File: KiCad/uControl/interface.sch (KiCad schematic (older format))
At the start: 41 parts, among them P10 C3SB, P11 VSel_Vlv, P12 Valve_Conn, P13 Valve_Conn_BO, P14 Valve, P15 Flow_Conn, P16 FlowMeter, P17 Pump_Conn, P18 Pump_Conn_BO, P19 Pump_Conn_Flex, P20 Temp_Conn, P21 Temp_Conn_BO, P22 Temp, P23 Pump, P6 Pulse, P7 Gage_Pr, P8 Abso_Pr, P9 C3SB, Q1 2SD1834T100, U1 TXB0104D, U2 TXS0102DCT

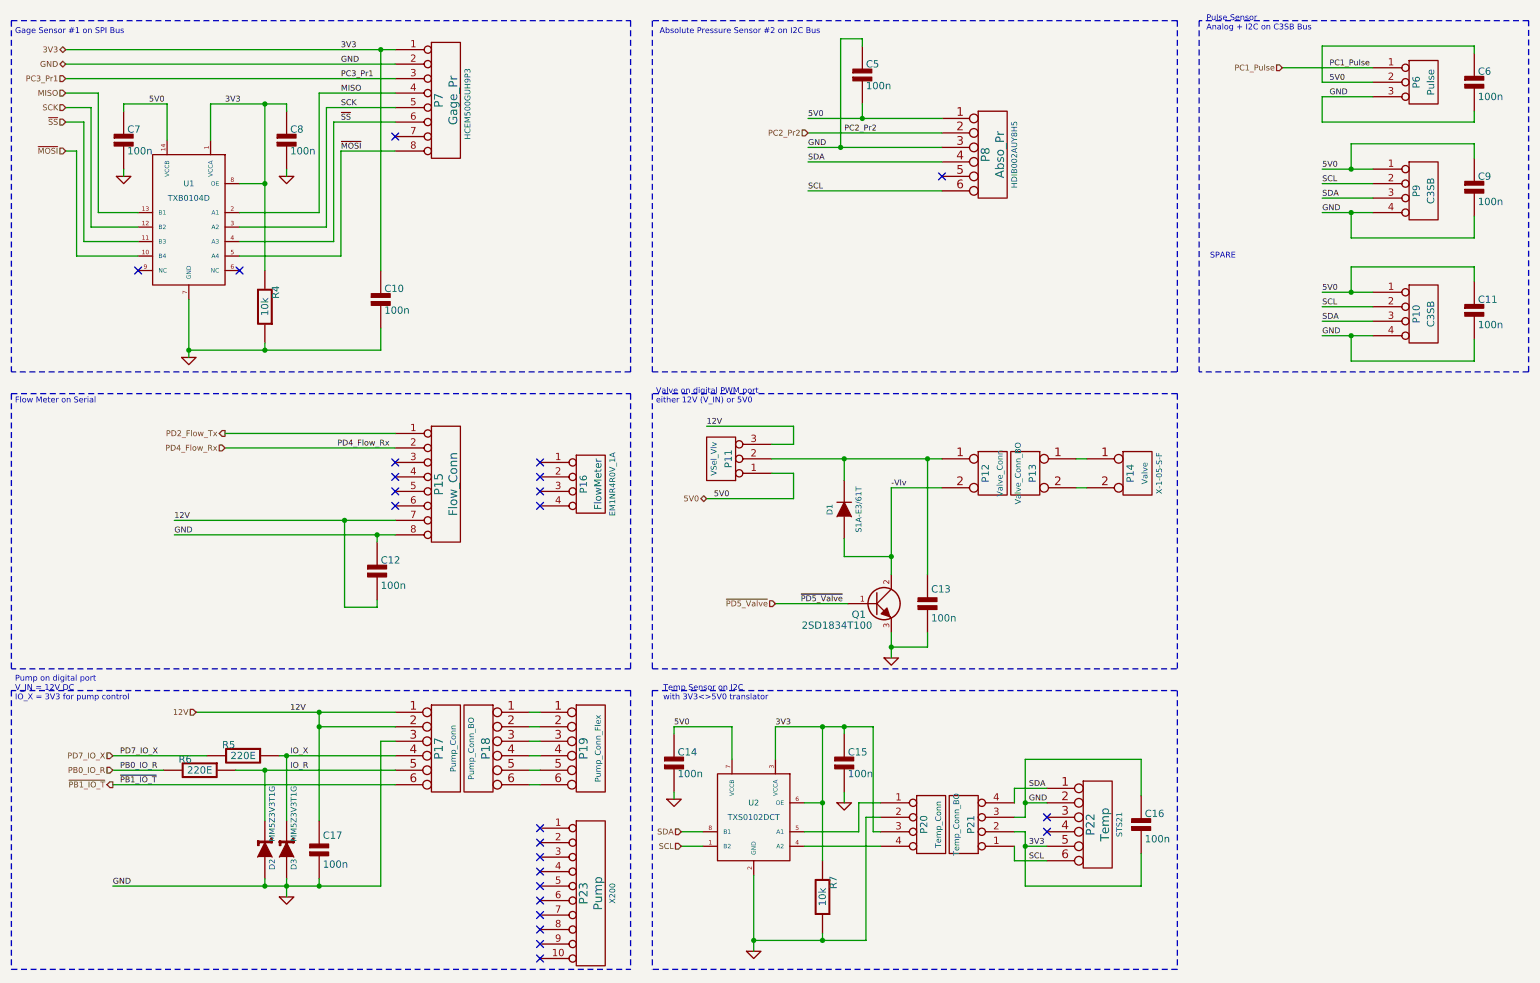
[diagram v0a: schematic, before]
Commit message: uControl footprints done. working on initial board layout
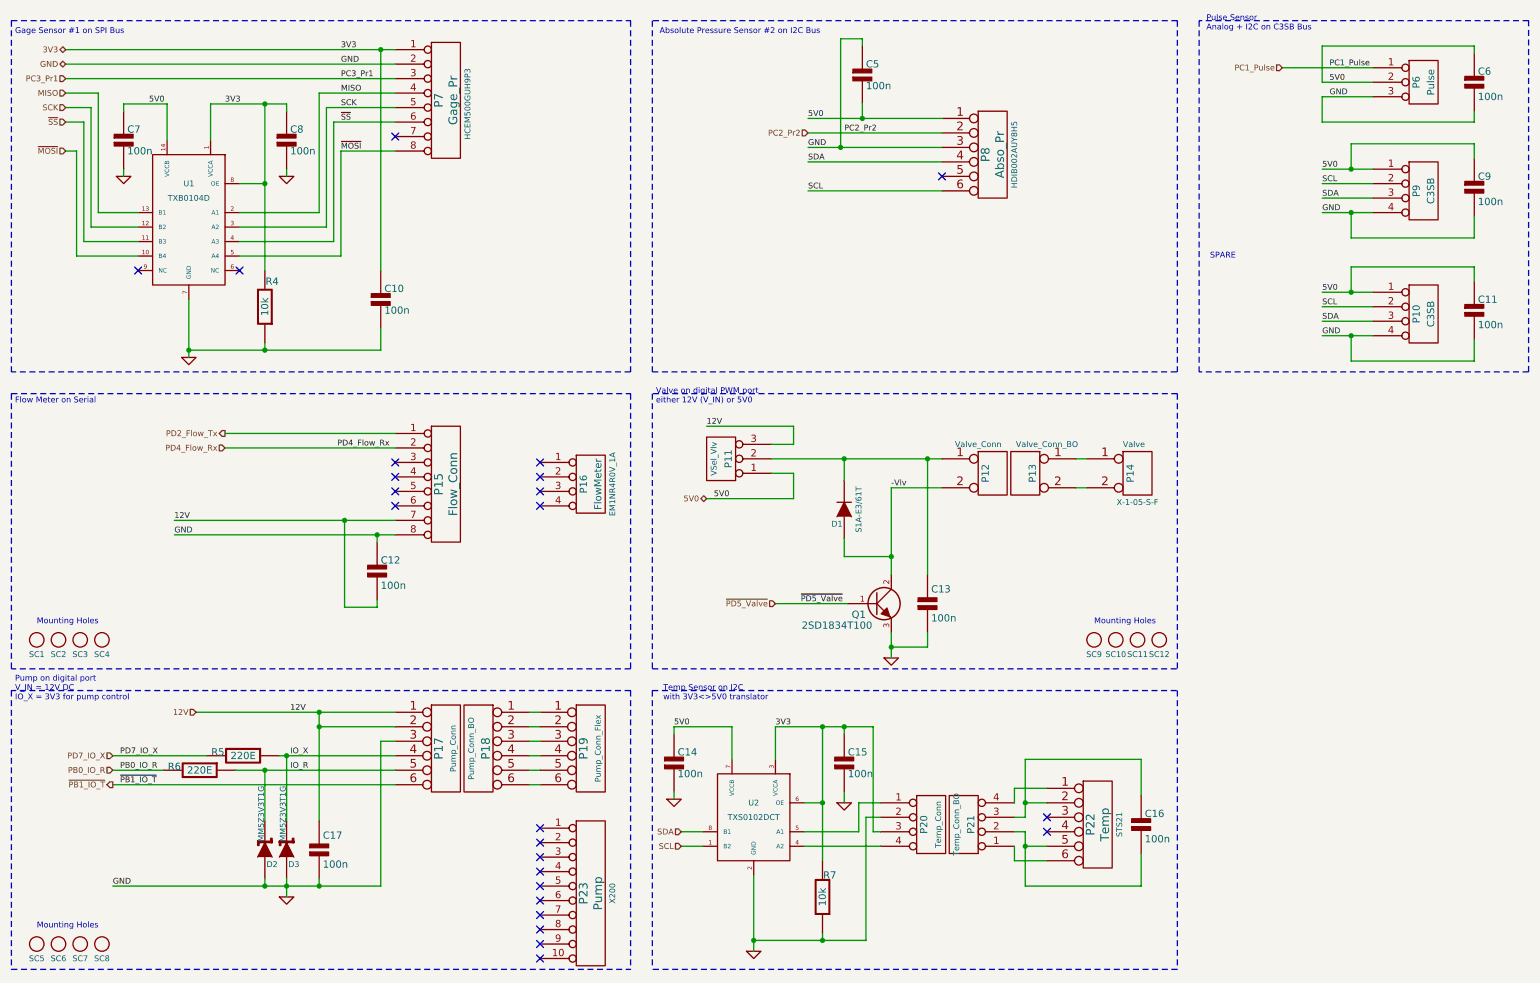
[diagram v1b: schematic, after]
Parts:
- added SC1, SC10, SC11, SC12, SC2, SC3, SC4, SC5, SC6, SC7, SC8, SC9: SCREW, vite_3mm, symbol SCREW
- D1: footprint diode-DO214AA -> S1A-E3
- D2, D3: footprint diode-DO214AA -> MM5Z3V3T1G
- P20, P21: footprint SIL-4 -> Header_2x2
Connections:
- net 3V3: no longer C16.2, P21.2 (P2), P22.5
- net GND: no longer C16.1, P21.3 (P3), P22.2
- net SCL: no longer P21.1 (P1), P22.6
- net SDA: no longer P21.4 (P4), P22.1
- new net: P21.4 (P4), P22.1
- new net: C16.1, P21.3 (P3), P22.2
- new net: C16.2, P21.2 (P2), P22.5
- new net: P21.1 (P1), P22.6
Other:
- note added: "Mounting Holes"
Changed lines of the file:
@@
-EESchema Schematic File Version 2  date Monday 24 December 2012 10:32:09 PM IST
+EESchema Schematic File Version 2  date 12/25/2012 5:14:27 PM
 LIBS:uControl
 LIBS:Conn-raspberry
@@
 Sheet 2 5
 Title ""
-Date "24 dec 2012"
+Date "25 dec 2012"
 Rev ""
 Comp ""
@@
 Comment4 ""
 $EndDescr
+$Comp
+L SCREW SC9
+U 1 1 50D99159
+P 8150 4850
+F 0 "SC9" H 8150 4750 40  0000 C CNN
+F 1 "SCREW" H 8150 4950 40  0001 C CNN
+F 2 "vite_3mm" H 8150 5050 40  0001 C CNN
+	1    8150 4850
+	1    0    0    -1
+$EndComp
+$Comp
+L SCREW SC10
+U 1 1 50D99158
+P 8300 4850
+F 0 "SC10" H 8300 4750 40  0000 C CNN
+F 1 "SCREW" H 8300 4950 40  0001 C CNN
+F 2 "vite_3mm" H 8300 5050 40  0001 C CNN
+	1    8300 4850
+	1    0    0    -1
+$EndComp
+$Comp
+L SCREW SC11
+U 1 1 50D99157
+P 8450 4850
+F 0 "SC11" H 8450 4750 40  0000 C CNN
+F 1 "SCREW" H 8450 4950 40  0001 C CNN
+F 2 "vite_3mm" H 8450 5050 40  0001 C CNN
+	1    8450 4850
+	1    0    0    -1
+$EndComp
+$Comp
+L SCREW SC12
+U 1 1 50D99156
+P 8600 4850
+F 0 "SC12" H 8600 4750 40  0000 C CNN
+F 1 "SCREW" H 8600 4950 40  0001 C CNN
+F 2 "vite_3mm" H 8600 5050 40  0001 C CNN
+	1    8600 4850
+	1    0    0    -1
+$EndComp
+Text Notes 8150 4750 0    40   ~ 0
+Mounting Holes
+$Comp
+L SCREW SC5
+U 1 1 50D99149
+P 850 6950
+F 0 "SC5" H 850 6850 40  0000 C CNN
+F 1 "SCREW" H 850 7050 40  0001 C CNN
+F 2 "vite_3mm" H 850 7150 40  0001 C CNN
+	1    850  6950
+	1    0    0    -1
+$EndComp
+$Comp
+L SCREW SC6
+U 1 1 50D99148
+P 1000 6950
+F 0 "SC6" H 1000 6850 40  0000 C CNN
+F 1 "SCREW" H 1000 7050 40  0001 C CNN
+F 2 "vite_3mm" H 1000 7150 40  0001 C CNN
+	1    1000 6950
+	1    0    0    -1
+$EndComp
+$Comp
+L SCREW SC7
+U 1 1 50D99147
+P 1150 6950
+F 0 "SC7" H 1150 6850 40  0000 C CNN
+F 1 "SCREW" H 1150 7050 40  0001 C CNN
+F 2 "vite_3mm" H 1150 7150 40  0001 C CNN
+	1    1150 6950
+	1    0    0    -1
+$EndComp
+$Comp
+L SCREW SC8
+U 1 1 50D99146
+P 1300 6950
+F 0 "SC8" H 1300 6850 40  0000 C CNN
+F 1 "SCREW" H 1300 7050 40  0001 C CNN
+F 2 "vite_3mm" H 1300 7150 40  0001 C CNN
+	1    1300 6950
+	1    0    0    -1
+$EndComp
+Text Notes 850  6850 0    40   ~ 0
+Mounting Holes
+Text Notes 850  4750 0    40   ~ 0
+Mounting Holes
+$Comp
+L SCREW SC4
+U 1 1 50D990FE
+P 1300 4850
+F 0 "SC4" H 1300 4750 40  0000 C CNN
+F 1 "SCREW" H 1300 4950 40  0001 C CNN
+F 2 "vite_3mm" H 1300 5050 40  0001 C CNN
+	1    1300 4850
+	1    0    0    -1
+$EndComp
+$Comp
+L SCREW SC3
+U 1 1 50D990FC
+P 1150 4850
+F 0 "SC3" H 1150 4750 40  0000 C CNN
+F 1 "SCREW" H 1150 4950 40  0001 C CNN
+F 2 "vite_3mm" H 1150 5050 40  0001 C CNN
+	1    1150 4850
+	1    0    0    -1
+$EndComp
+$Comp
+L SCREW SC2
+U 1 1 50D990F9
+P 1000 4850
+F 0 "SC2" H 1000 4750 40  0000 C CNN
+F 1 "SCREW" H 1000 4950 40  0001 C CNN
+F 2 "vite_3mm" H 1000 5050 40  0001 C CNN
+	1    1000 4850
+	1    0    0    -1
+$EndComp
+$Comp
+L SCREW SC1
+U 1 1 50D990F0
+P 850 4850
+F 0 "SC1" H 850 4750 40  0000 C CNN
+F 1 "SCREW" H 850 4950 40  0001 C CNN
+F 2 "vite_3mm" H 850 5050 40  0001 C CNN
+	1    850  4850
+	1    0    0    -1
+$EndComp
 Wire Wire Line
 	8025 3800 8100 3800
@@
 P 8450 3700
 F 0 "P14" V 8400 3700 50  0000 C CNN
-F 1 "Valve" V 8500 3700 40  0000 C CNN
+F 1 "Valve" H 8425 3900 40  0000 C CNN
 F 2 "Valve" V 8600 3700 40  0001 C CNN
-F 4 "X-1-05-S-F" V 8600 3700 40  0000 C CNN "Part_No"
+F 4 "X-1-05-S-F" H 8450 3500 40  0000 C CNN "Part_No"
 	1    8450 3700
 	1    0    0    -1
@@
 P 7675 3700
 F 0 "P13" V 7625 3700 50  0000 C CNN
-F 1 "Valve_Conn_BO" V 7725 3700 40  0000 C CNN
+F 1 "Valve_Conn_BO" H 7525 3900 40  0000 C CNN
 F 2 "Header_5V_Link" V 7825 3700 40  0001 C CNN
 F 4 "X-1-05-S-F" V 7825 3700 40  0001 C CNN "Part_No"
@@
 P 7450 3700
 F 0 "P12" V 7400 3700 50  0000 C CNN
-F 1 "Valve_Conn" V 7500 3700 40  0000 C CNN
+F 1 "Valve_Conn" H 7350 3900 40  0000 C CNN
 F 2 "Header_5V_Link" V 7600 3700 40  0001 C CNN
 F 4 "X-1-05-S-F" V 7600 3700 40  0001 C CNN "Part_No"
@@
 F 0 "P21" V 7200 6125 50  0000 C CNN
 F 1 "Temp_Conn_BO" V 7300 6125 40  0000 C CNN
-F 2 "SIL-4" V 7400 6125 40  0001 C CNN
+F 2 "Header_2x2" V 7400 6125 40  0001 C CNN
 	1    7250 6125
 	-1   0    0    1
@@
 F 0 "P20" V 6975 6125 50  0000 C CNN
 F 1 "Temp_Conn" V 7075 6125 40  0000 C CNN
-F 2 "SIL-4" V 7175 6125 40  0001 C CNN
+F 2 "Header_2x2" V 7175 6125 40  0001 C CNN
 	1    7025 6125
 	1    0    0    -1
@@
 U 1 1 50CCC247
 P 6275 6625
-F 0 "R7" V 6200 6525 50  0000 C CNN
+F 0 "R7" H 6225 6475 50  0000 C CNN
 F 1 "10k" V 6275 6625 50  0000 C CNN
 F 2 "r_0805" V 6375 6625 50  0001 C CNN
@@
 U 1 1 50CCC15C
 P 2425 2550
-F 0 "R4" V 2350 2450 50  0000 C CNN
+F 0 "R4" H 2375 2375 50  0000 C CNN
 F 1 "10k" V 2425 2550 50  0000 C CNN
 F 2 "r_0805" V 2525 2550 50  0001 C CNN
@@
 Text HLabel 9450 900  0    40   Input ~ 0
 PC1_Pulse
-Text Label 7700 6375 0    40   ~ 0
-SCL
-Text Label 7700 5875 0    40   ~ 0
-SDA
 NoConn ~ 7825 6175
 NoConn ~ 7825 6075
@@
 	1    0    0    -1
 $EndComp
-Text Label 7700 5975 0    40   ~ 0
-GND
-Text Label 7700 6275 0    40   ~ 0
-3V3
 Text Label 9775 900  0    40   ~ 0
 PC1_Pulse
@@
 U 1 1 50BA3BBD
 P 2425 6300
-F 0 "D2" H 2325 6250 40  0000 C CNN
-F 1 "MM5Z3V3T1G" H 2675 6250 40  0000 C CNN
-F 2 "diode-DO214AA" H 2675 6350 40  0001 C CNN
+F 0 "D2" V 2325 6250 40  0000 C CNN
+F 1 "MM5Z3V3T1G" H 2675 6325 40  0000 C CNN
+F 2 "MM5Z3V3T1G" H 2675 6350 40  0001 C CNN
 	1    2425 6300
 	0    -1   -1   0
@@
 U 1 1 50BA3B80
 P 1975 5750
-F 0 "R6" V 1900 5650 50  0000 C CNN
+F 0 "R6" V 1950 5575 50  0000 C CNN
 F 1 "220E" V 1975 5750 50  0000 C CNN
 F 2 "r_0805" V 2075 5750 50  0001 C CNN
@@
 U 1 1 50B7155C
 P 6425 3950
-F 0 "D1" H 6425 4050 40  0000 C CNN
+F 0 "D1" V 6325 4000 40  0000 C CNN
 F 1 "S1A-E3/61T" H 6425 3850 40  0000 C CNN
-F 2 "diode-DO214AA" H 6425 3950 40  0001 C CNN
+F 2 "S1A-E3" H 6425 3950 40  0001 C CNN
 	1    6425 3950
 	0    -1   -1   0
@@
 U 1 1 50B22950
 P 2275 5650
-F 0 "R5" V 2200 5550 50  0000 C CNN
+F 0 "R5" V 2250 5475 50  0000 C CNN
 F 1 "220E" V 2275 5650 50  0000 C CNN
 F 2 "r_0805" V 2375 5650 50  0001 C CNN
@@
 U 1 1 50B22921
 P 2575 6300
-F 0 "D3" H 2475 6250 40  0000 C CNN
-F 1 "MM5Z3V3T1G" H 2825 6250 40  0000 C CNN
-F 2 "diode-DO214AA" H 2825 6350 40  0001 C CNN
+F 0 "D3" V 2475 6250 40  0000 C CNN
+F 1 "MM5Z3V3T1G" H 2825 6325 40  0000 C CNN
+F 2 "MM5Z3V3T1G" H 2825 6350 40  0001 C CNN
 	1    2575 6300
 	0    -1   -1   0

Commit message: uControl Board sizes defined. Manifold added. Can be single large board or smaller one with breakouts - both possible.
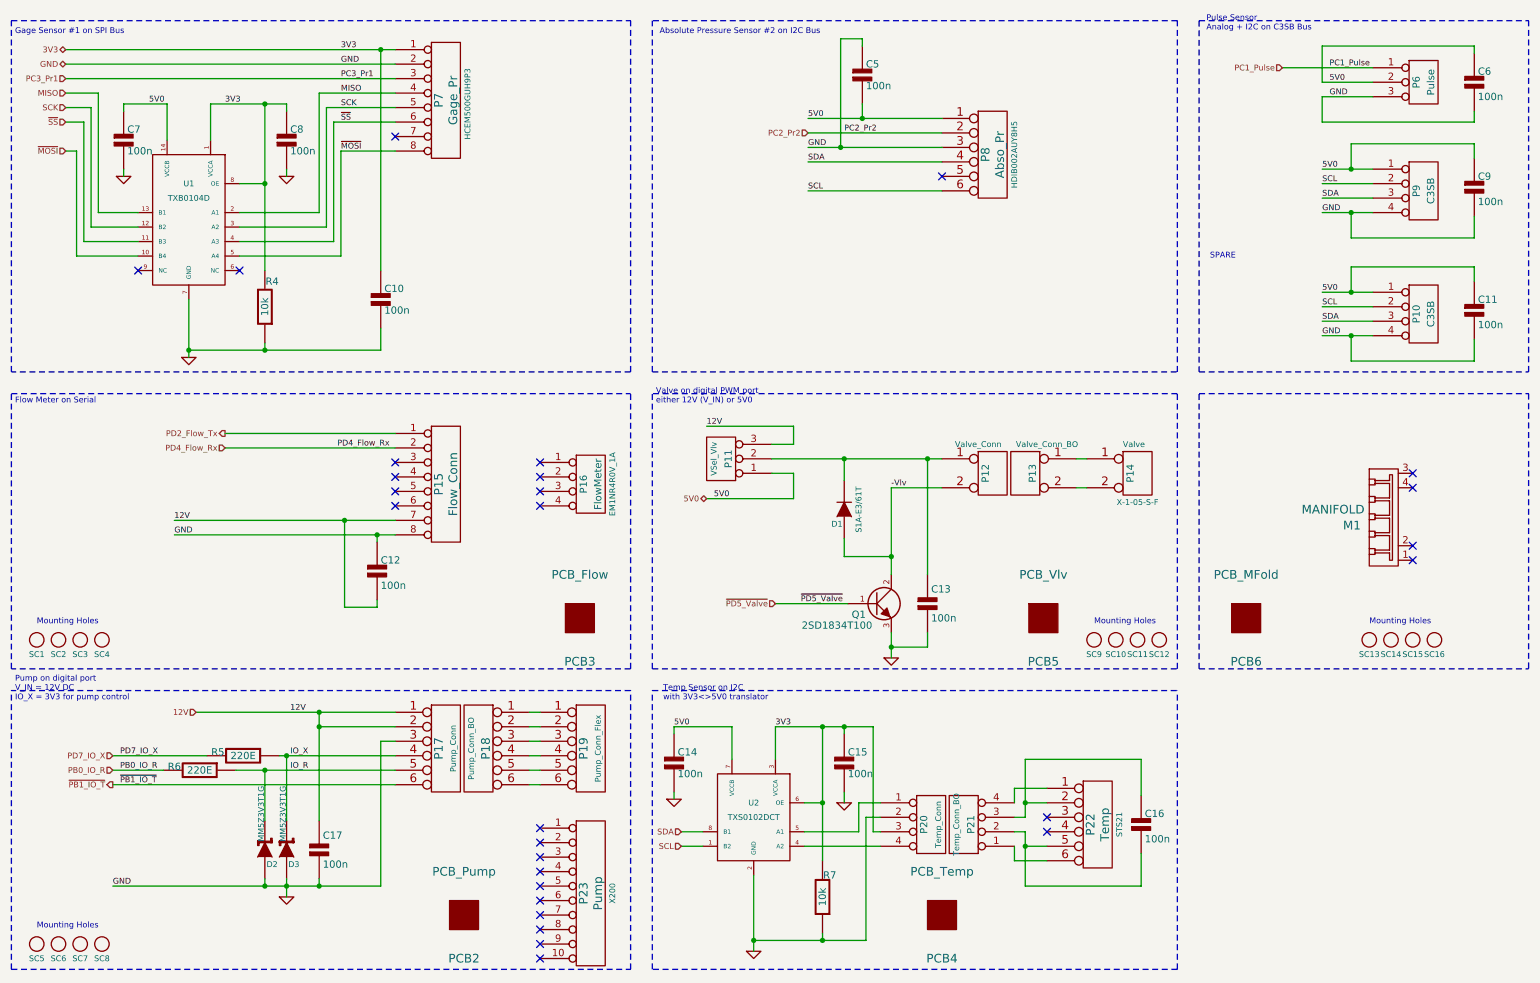
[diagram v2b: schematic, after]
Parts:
- added M1: MANIFOLD, Manifold, symbol MANIFOLD
- added PCB2: PCB_Pump, PCB_Pump, symbol PCB
- added PCB3: PCB_Flow, PCB_Flow, symbol PCB
- added PCB4: PCB_Temp, PCB_Temp, symbol PCB
- added PCB5: PCB_Vlv, PCB_Vlv, symbol PCB
- added PCB6: PCB_MFold, PCB_Mfold, symbol PCB
- added SC13, SC14, SC15, SC16: SCREW, vite_3mm, symbol SCREW
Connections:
- no-connect marks 24 -> 28

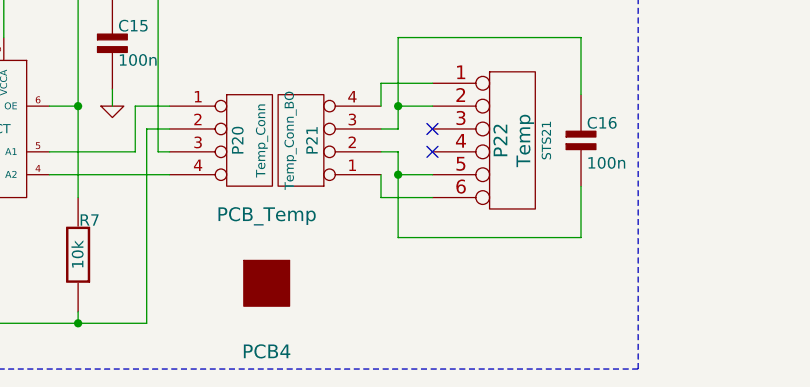
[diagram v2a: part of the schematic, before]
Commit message: uControl footprint layout almost done.
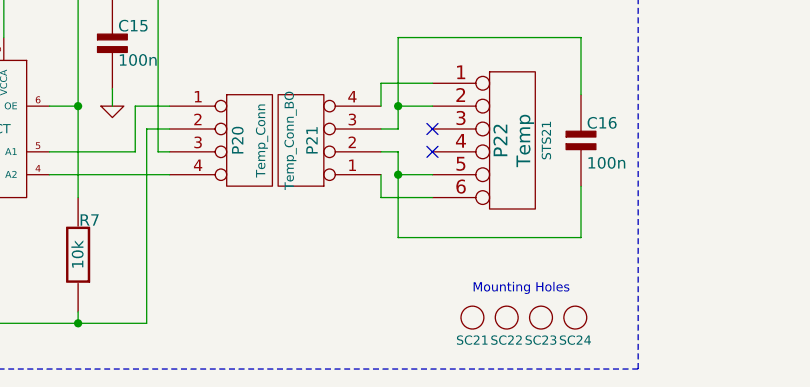
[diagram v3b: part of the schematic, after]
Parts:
- removed PCB4: PCB_Temp, PCB_Temp, symbol PCB
- added SC21, SC22, SC23, SC24: SCREW, vite_3mm, symbol SCREW
- M1: footprint Manifold -> Manifold2
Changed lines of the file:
@@
-EESchema Schematic File Version 2  date 12/26/2012 6:01:00 PM
+EESchema Schematic File Version 2  date 12/27/2012 6:53:46 PM
 LIBS:uControl
 LIBS:Conn-raspberry
@@
 Sheet 2 5
 Title ""
-Date "26 dec 2012"
+Date "27 dec 2012"
 Rev ""
 Comp ""
@@
 $EndDescr
 $Comp
+L SCREW SC21
+U 1 1 50DC1602
+P 8000 6900
+F 0 "SC21" H 8000 6800 40  0000 C CNN
+F 1 "SCREW" H 8000 7000 40  0001 C CNN
+F 2 "vite_3mm" H 8000 7100 40  0001 C CNN
+	1    8000 6900
+	1    0    0    -1
+$EndComp
+$Comp
+L SCREW SC22
+U 1 1 50DC1601
+P 8150 6900
+F 0 "SC22" H 8150 6800 40  0000 C CNN
+F 1 "SCREW" H 8150 7000 40  0001 C CNN
+F 2 "vite_3mm" H 8150 7100 40  0001 C CNN
+	1    8150 6900
+	1    0    0    -1
+$EndComp
+$Comp
+L SCREW SC23
+U 1 1 50DC1600
+P 8300 6900
+F 0 "SC23" H 8300 6800 40  0000 C CNN
+F 1 "SCREW" H 8300 7000 40  0001 C CNN
+F 2 "vite_3mm" H 8300 7100 40  0001 C CNN
+	1    8300 6900
+	1    0    0    -1
+$EndComp
+$Comp
+L SCREW SC24
+U 1 1 50DC15FF
+P 8450 6900
+F 0 "SC24" H 8450 6800 40  0000 C CNN
+F 1 "SCREW" H 8450 7000 40  0001 C CNN
+F 2 "vite_3mm" H 8450 7100 40  0001 C CNN
+	1    8450 6900
+	1    0    0    -1
+$EndComp
+Text Notes 8000 6800 0    40   ~ 0
+Mounting Holes
+$Comp
 L PCB PCB6
 U 1 1 50DAE3BE
@@
 $EndComp
 $Comp
-L PCB PCB4
-U 1 1 50DAE3A1
-P 7100 6750
-F 0 "PCB4" H 7100 6450 60  0000 C CNN
-F 1 "PCB_Temp" H 7100 7050 60  0000 C CNN
-F 2 "PCB_Temp" H 7100 7150 60  0001 C CNN
-	1    7100 6750
-	1    0    0    -1
-$EndComp
-$Comp
 L PCB PCB2
 U 1 1 50DAE394
@@
 F 0 "M1" H 9930 3940 60  0000 C CNN
 F 1 "MANIFOLD" H 9800 4050 60  0000 C CNN
-F 2 "Manifold" H 9800 4150 60  0001 C CNN
+F 2 "Manifold2" H 9800 4150 60  0001 C CNN
 	1    10150 4000
 	1    0    0    -1
@@
 $EndComp
 $Comp
-L GND #PWR8
+L GND #PWR03
 U 1 1 50CCC2AC
 P 6425 5975
-F 0 "#PWR8" H 6425 5975 30  0001 C CNN
+F 0 "#PWR03" H 6425 5975 30  0001 C CNN
 F 1 "GND" H 6425 5905 30  0001 C CNN
 	1    6425 5975
@@
 $EndComp
 $Comp
-L GND #PWR6
+L GND #PWR04
 U 1 1 50CCC292
 P 5250 5950
-F 0 "#PWR6" H 5250 5950 30  0001 C CNN
+F 0 "#PWR04" H 5250 5950 30  0001 C CNN
 F 1 "GND" H 5250 5880 30  0001 C CNN
 	1    5250 5950
@@
 5V0
 $Comp
-L GND #PWR7
+L GND #PWR05
 U 1 1 50CCC1EF
 P 5800 7000
-F 0 "#PWR7" H 5800 7000 30  0001 C CNN
+F 0 "#PWR05" H 5800 7000 30  0001 C CNN
 F 1 "GND" H 5800 6930 30  0001 C CNN
 	1    5800 7000
@@
 $EndComp
 $Comp
-L GND #PWR4
+L GND #PWR06
 U 1 1 50CCABF0
 P 2575 1650
-F 0 "#PWR4" H 2575 1650 30  0001 C CNN
+F 0 "#PWR06" H 2575 1650 30  0001 C CNN
 F 1 "GND" H 2575 1580 30  0001 C CNN
 	1    2575 1650
@@
 $EndComp
 $Comp
-L GND #PWR2
+L GND #PWR07
 U 1 1 50CCABEC
 P 1450 1650
-F 0 "#PWR2" H 1450 1650 30  0001 C CNN
+F 0 "#PWR07" H 1450 1650 30  0001 C CNN
 F 1 "GND" H 1450 1580 30  0001 C CNN
 	1    1450 1650
@@
 $EndComp
 $Comp
-L GND #PWR3
+L GND #PWR08
 U 1 1 50CCAA70
 P 1900 2900
-F 0 "#PWR3" H 1900 2900 30  0001 C CNN
+F 0 "#PWR08" H 1900 2900 30  0001 C CNN
 F 1 "GND" H 1900 2830 30  0001 C CNN
 	1    1900 2900
@@
 12V
 $Comp
-L GND #PWR9
+L GND #PWR09
 U 1 1 50B4B058
 P 6750 4975
-F 0 "#PWR9" H 6750 4975 30  0001 C CNN
+F 0 "#PWR09" H 6750 4975 30  0001 C CNN
 F 1 "GND" H 6750 4905 30  0001 C CNN
 	1    6750 4975
@@
 $EndComp
 $Comp
-L GND #PWR5
+L GND #PWR010
 U 1 1 50B4B052
 P 2575 6625
-F 0 "#PWR5" H 2575 6625 30  0001 C CNN
+F 0 "#PWR010" H 2575 6625 30  0001 C CNN
 F 1 "GND" H 2575 6555 30  0001 C CNN
 	1    2575 6625
